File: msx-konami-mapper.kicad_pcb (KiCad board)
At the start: 2 copper layers, 65.3 x 63 mm, 6 parts, among them SW1 High/Low, U1 SST39SF040, U3 74LS670

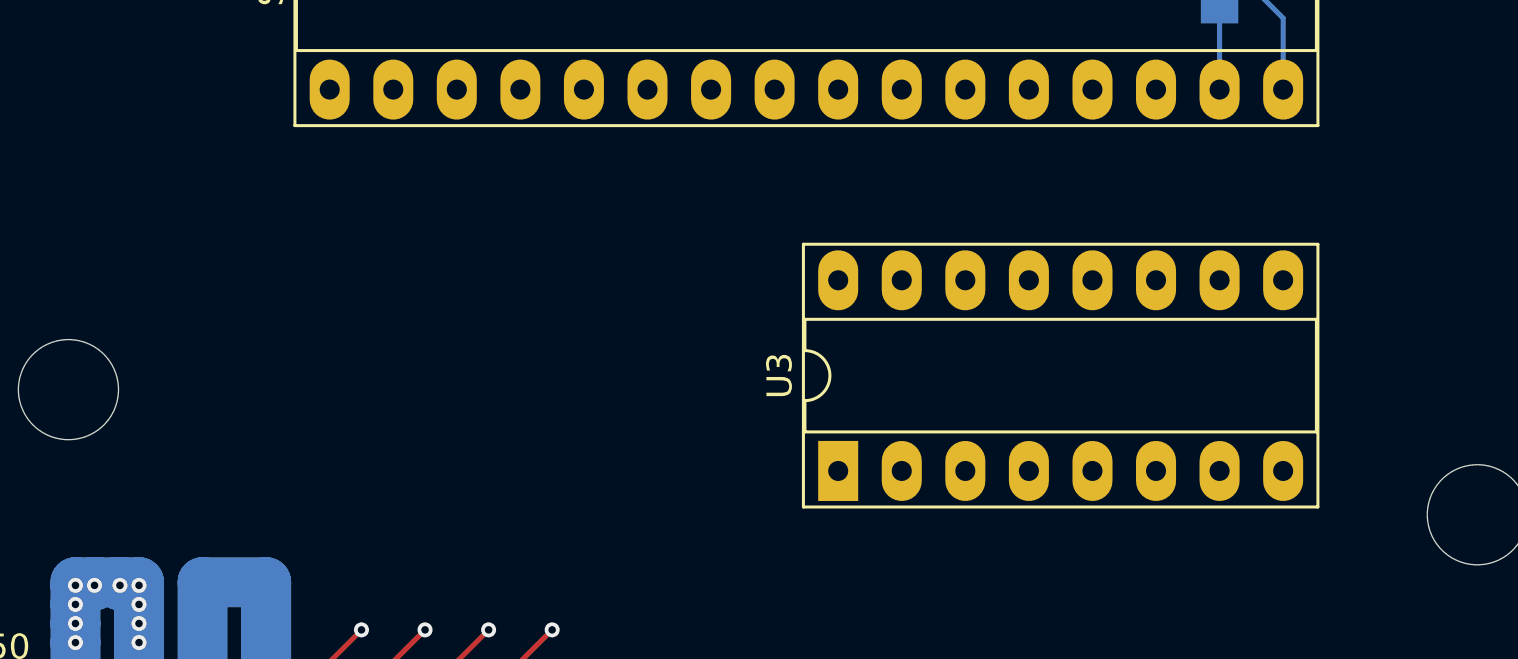
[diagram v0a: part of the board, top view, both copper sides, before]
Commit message: Driving 8 bits of pages
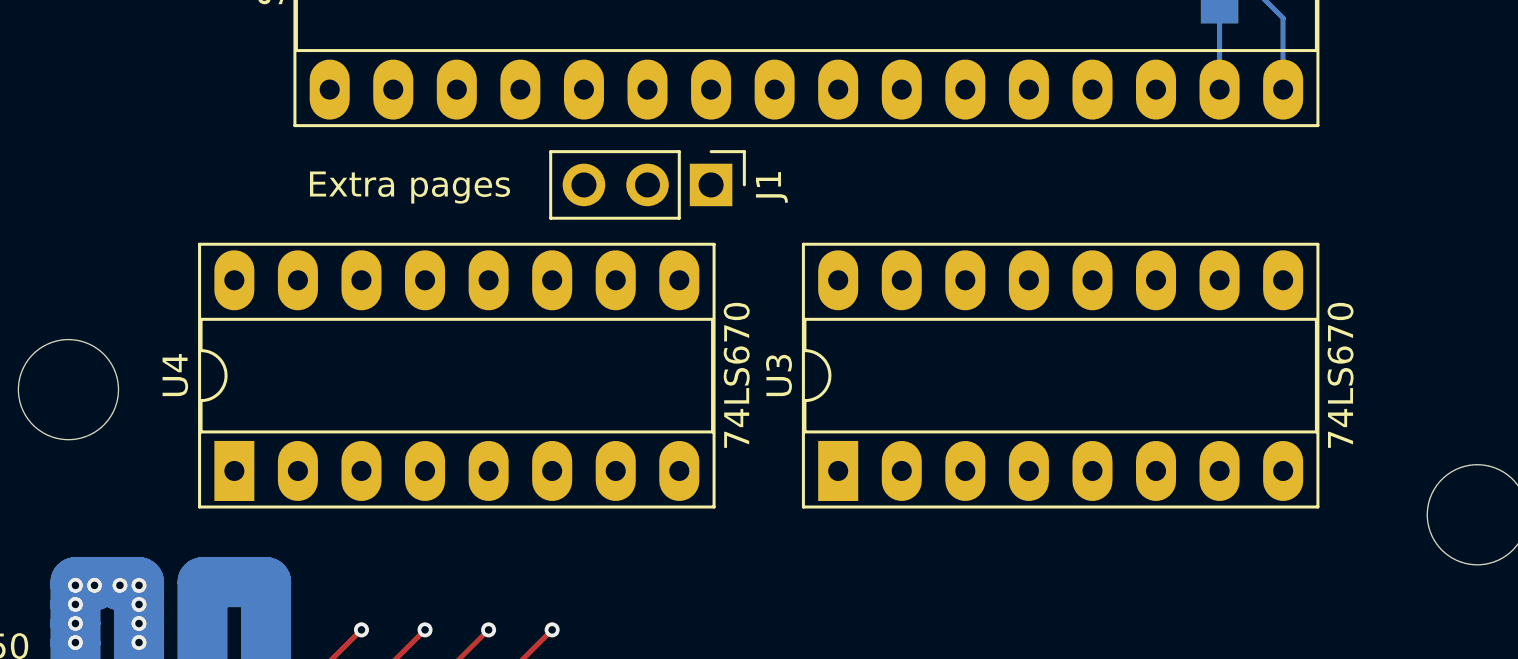
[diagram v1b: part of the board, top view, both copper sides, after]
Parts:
- added J1: Extra pages, Connector_PinHeader_2.54mm:PinHeader_1x03_P2.54mm_Vertical, F.Cu at (170.2, 83.8)
- added U4: 74LS670, Package_DIP:DIP-16_W7.62mm_Socket_LongPads, F.Cu at (151.1, 95.2)
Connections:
- net /PA18 renamed /Game_Select
- U3 pad 1: unconnected-(U3-D2-Pad1) -> /D1
- U3 pad 10: unconnected-(U3-Q1-Pad10) -> /PA13
- U3 pad 11: unconnected-(U3-~{Er}-Pad11) -> /~{PAGED_READ}
- U3 pad 12: unconnected-(U3-~{Ew}-Pad12) -> /~{PAGE_WRITE}
- U3 pad 15: unconnected-(U3-D1-Pad15) -> /D0
- U3 pad 2: unconnected-(U3-D3-Pad2) -> /D2
- U3 pad 3: unconnected-(U3-D4-Pad3) -> /D3
- U3 pad 6: unconnected-(U3-Q4-Pad6) -> /PA16
- U3 pad 7: unconnected-(U3-Q3-Pad7) -> /PA15
- U3 pad 9: unconnected-(U3-Q2-Pad9) -> /PA14

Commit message: I think this works
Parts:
- removed J1: Extra pages, Connector_PinHeader_2.54mm:PinHeader_1x03_P2.54mm_Vertical
- added C1: 0.1µF, Capacitor_THT:C_Disc_D3.8mm_W2.6mm_P2.50mm, F.Cu at (129.2, 80.2)
- added C2: 0.1µF, Capacitor_THT:C_Disc_D3.8mm_W2.6mm_P2.50mm, F.Cu at (129.2, 84.4)
- added C3: 0.1µF, Capacitor_THT:C_Disc_D3.8mm_W2.6mm_P2.50mm, F.Cu at (129.2, 88.5)
- added R1: 10kΩ, Resistor_THT:R_Axial_DIN0207_L6.3mm_D2.5mm_P10.16mm_Horizontal, F.Cu at (117.4, 62.0)
- added R2: 10kΩ, Resistor_THT:R_Axial_DIN0207_L6.3mm_D2.5mm_P10.16mm_Horizontal, F.Cu at (117.4, 66.8)
- SW1: value High/Low -> Bonus Games; footprint Connector_PinHeader_2.54mm:PinHeader_1x03_P2.54mm_Vertical -> Button_Switch_THT:SW_DIP_SPSTx02_Slide_9.78x7.26mm_W7.62mm_P2.54mm
- U4: value 74LS670 -> 74LS02; footprint Package_DIP:DIP-16_W7.62mm_Socket_LongPads -> Package_DIP:DIP-14_W7.62mm_Socket_LongPads
- moved SW1 12.3 mm to (198.4, 83.8), turned to 90 degrees
- moved U4 2.54 mm to (153.7, 95.2)
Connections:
- SW1 pad 1: +5V -> GND
- SW1 pad 2: /Game_Select -> GND
- SW1 pad 3: GND -> +5V
- U1 pad 1: /Game_Select -> +5V
- U1 pad 22: unconnected-(U1-CE-Pad22) -> /~{SLTSL}
- U1 pad 24: unconnected-(U1-OE-Pad24) -> /~{RD}
- U1 pad 30: /PA17 -> Net-(U1-A17)
- U2 pad 13: unconnected-(U2-~{WR}-Pad13) -> /~{WR}
- U2 pad 18: unconnected-(U2-A15-Pad18) -> /A15
- U2 pad 25: unconnected-(U2-A14-Pad25) -> /A14
- U2 pad 4: unconnected-(U2-~{SLTSL}-Pad4) -> /~{SLTSL}
- U3 pad 1: /D1 -> /D2
- U3 pad 10: /PA13 -> /PA16
- U3 pad 13: unconnected-(U3-Wb-Pad13) -> /A13
- U3 pad 14: unconnected-(U3-Wa-Pad14) -> /A15
- U3 pad 15: /D0 -> /D3
- U3 pad 2: /D2 -> /D1
- U3 pad 3: /D3 -> /D0
- U3 pad 4: unconnected-(U3-Rb-Pad4) -> /A13
- U3 pad 5: unconnected-(U3-Ra-Pad5) -> /A15
- U3 pad 6: /PA16 -> /PA13
- U3 pad 7: /PA15 -> /PA14
- U3 pad 9: /PA14 -> /PA15
- U4 pad 1: /D6 -> Net-(U4-Pad1)
- U4 pad 10: /PA17 -> /~{PAGED_READ}
- U4 pad 11: /~{PAGED_READ} -> GND
- U4 pad 12: /~{PAGE_WRITE} -> GND
- U4 pad 14: unconnected-(U4-Wa-Pad14) -> +5V
- U4 pad 2: /D7 -> /~{WR}
- U4 pad 3: /D8 -> /~{SLTSL}
- U4 pad 4: unconnected-(U4-Rb-Pad4) -> /~{PAGE_WRITE}
- U4 pad 5: unconnected-(U4-Ra-Pad5) -> Net-(U4-Pad1)
- U4 pad 6: /PA20 -> Net-(U4-Pad1)
- U4 pad 7: /PA19 -> GND
- U4 pad 8: GND -> /A15
- U4 pad 9: /PA18 -> /A13
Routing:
- net +5V: track 25.3 -> 0.00 mm, vias 10 -> 0
- net GND: track 19.1 -> 0.00 mm
- net /Game_Select: track 12.1 -> 0.00 mm, vias 1 -> 0
- net Net-(U2-SW1): track 12.0 -> 0.00 mm
- net /D6: track 6.88 -> 0.00 mm, vias 1 -> 0
- net /D4: track 6.88 -> 0.00 mm, vias 1 -> 0
- net /D0: track 6.88 -> 0.00 mm, vias 1 -> 0
- net /D2: track 6.88 -> 0.00 mm, vias 1 -> 0
- net Net-(JP1-B): track 3.15 -> 0.00 mm
- net /D3: track 0.90 -> 0.00 mm

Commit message: Routed
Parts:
- moved R2 83.9 mm to (201.3, 63.5), turned to -90 degrees
- moved R1 80.7 mm to (198.1, 63.5), turned to -90 degrees
- moved C1 73.5 mm to (201.9, 90.8), turned to -90 degrees
- moved C2 26.3 mm to (148.6, 66.7), turned to 90 degrees
- moved C3 19.7 mm to (148.6, 85.1), turned to -90 degrees
- moved U3 1.91 mm to (175.3, 93.3)
- moved U4 1.91 mm to (153.7, 93.3)
- moved JP1 0.65 mm to (190.5, 75.6)
- moved U1 0.63 mm to (193.0, 64.1)
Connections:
- R2 pad 2: +5V -> Net-(U1-A18)
- SW1 pad 3: +5V -> Net-(U1-A18)
- U1 pad 1: +5V -> Net-(U1-A18)
- U2 pad 14: unconnected-(U2-~{RD}-Pad14) -> /~{RD}
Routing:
- net /A1: track 0.00 -> 120.7 mm, vias 0 -> 7
- net /A8: track 0.00 -> 112.7 mm, vias 0 -> 4
- net /~{SLTSL}: track 0.00 -> 95.6 mm, vias 0 -> 6
- net /A5: track 0.00 -> 92.8 mm, vias 0 -> 7
- net /D0: track 0.00 -> 87.7 mm, vias 0 -> 8
- net /A3: track 0.00 -> 83.5 mm, vias 0 -> 5
- net /A11: track 0.00 -> 81.7 mm, vias 0 -> 5
- net /D1: track 0.00 -> 78.2 mm, vias 0 -> 5
- net /D2: track 0.00 -> 76.1 mm, vias 0 -> 4
- net /~{RD}: track 0.00 -> 74.4 mm, vias 0 -> 4
- net +5V: track 0.00 -> 73.8 mm, vias 0 -> 14
- net /D3: track 0.00 -> 71.9 mm, vias 0 -> 5
- net /A6: track 0.00 -> 61.8 mm, vias 0 -> 4
- net GND: track 0.00 -> 60.5 mm, vias 0 -> 3
- net /A4: track 0.00 -> 54.3 mm, vias 0 -> 4
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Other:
- board text added: "MSX rules"

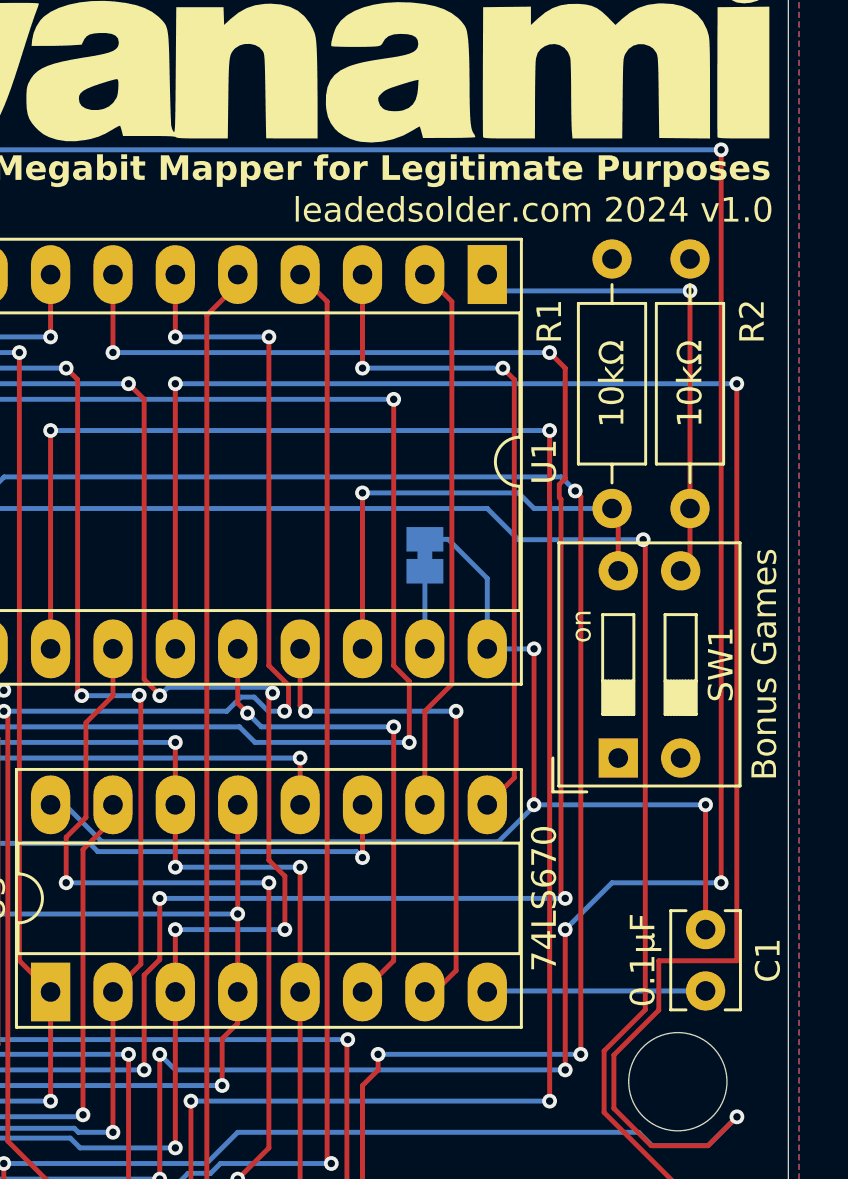
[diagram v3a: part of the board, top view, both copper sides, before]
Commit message: V1.1 begins... worried about C1 being too close to mounting hole
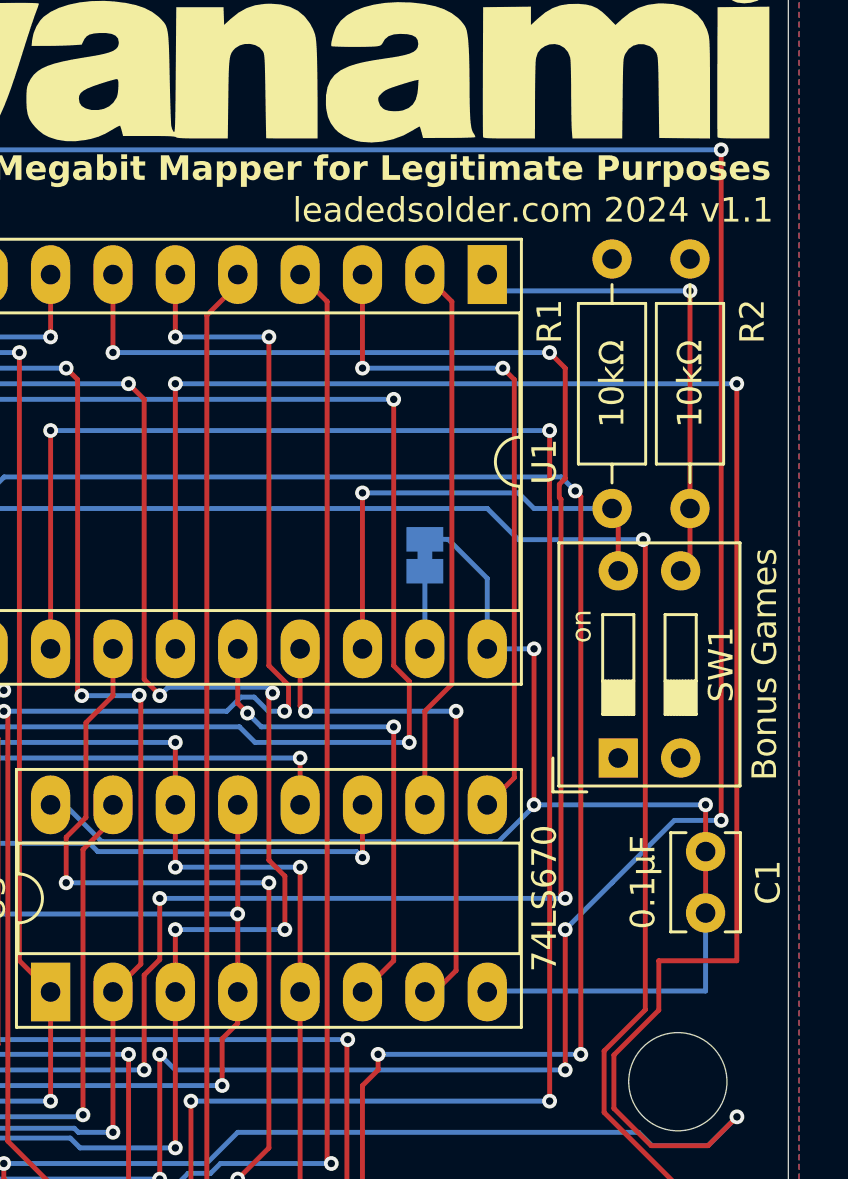
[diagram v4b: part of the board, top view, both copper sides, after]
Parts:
- moved C1 3.18 mm to (201.9, 87.6)
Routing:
- net GND: track 60.5 -> 63.7 mm
- net /A1: track 120.7 -> 119.2 mm
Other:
- board text added: "leadedsolder.com 2024 v1.1"
- board text removed: "leadedsolder.com 2024 v1.0"
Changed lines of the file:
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@@
 			(outputformat 1)
 			(mirror no)
-			(drillshape 1)
+			(drillshape 0)
 			(scaleselection 1)
-			(outputdirectory "")
+			(outputdirectory "msx-megarom-v1")
 		)
 	)
@@
 		)
 		(fp_text user "${REFERENCE}"
-			(at 7.27 1.27 360)
+			(at 7.27 1.27 0)
 			(layer "F.Fab")
 			(effects
@@
 	(footprint "Capacitor_THT:C_Disc_D3.8mm_W2.6mm_P2.50mm"
 		(layer "F.Cu")
-		(at 201.93 90.805 -90)
+		(at 201.93 87.63 -90)
 		(descr "C, Disc series, Radial, pin pitch=2.50mm, , diameter*width=3.8*2.6mm^2, Capacitor, http://www.vishay.com/docs/45233/krseries.pdf")
 		(tags "C Disc series Radial pin pitch 2.50mm  diameter 3.8mm width 2.6mm Capacitor")
@@
 		)
 	)
-	(gr_text "leadedsolder.com 2024 v1.0"
+	(gr_text "leadedsolder.com 2024 v1.1"
 		(at 204.7 62.1 0)
 		(layer "F.SilkS")
@@
 	)
 	(segment
-		(start 167.64 59.055)
-		(end 167.64 64.135)
+		(start 202.565 86.36)
+		(end 202.565 59.055)
 		(width 0.2)
 		(layer "F.Cu")
@@
 	)
 	(segment
-		(start 196.215 96.52)
-		(end 196.215 90.805)
+		(start 167.64 59.055)
+		(end 167.64 64.135)
 		(width 0.2)
 		(layer "F.Cu")
@@
 	)
 	(segment
-		(start 202.565 88.9)
-		(end 202.565 59.055)
+		(start 196.215 96.52)
+		(end 196.215 90.805)
 		(width 0.2)
 		(layer "F.Cu")
@@
 	)
 	(via
-		(at 202.565 88.9)
+		(at 202.565 86.36)
 		(size 0.6)
 		(drill 0.3)
@@
 	)
 	(segment
+		(start 198.12 88.9)
+		(end 200.66 86.36)
+		(width 0.2)
+		(layer "B.Cu")
+		(net 26)
+	)
+	(segment
 		(start 179.705 95.885)
 		(end 180.34 96.52)
@@
 	)
 	(segment
+		(start 200.66 86.36)
+		(end 202.565 86.36)
+		(width 0.2)
+		(layer "B.Cu")
+		(net 26)
+	)
+	(segment
 		(start 170.815 100.965)
 		(end 179.705 100.965)
@@
 	)
 	(segment
-		(start 198.12 88.9)
-		(end 202.565 88.9)
-		(width 0.2)
-		(layer "B.Cu")
-		(net 26)
-	)
-	(segment
 		(start 170.18 101.6)
 		(end 170.815 100.965)
@@
 		(width 0.2)
 		(layer "B.Cu")
+		(net 48)
+	)
+	(segment
+		(start 201.93 93.305)
+		(end 201.93 90.13)
+		(width 0.2)
+		(layer "B.Cu")
